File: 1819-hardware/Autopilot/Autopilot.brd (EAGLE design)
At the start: 44.4 x 54 mm, 36 parts, among them U1 PCA9615, U2 PCA9306, U3 74HC1G04, U4 MAX3485CSA, U5 V_REG_LD1117VXXLD1117-SMD

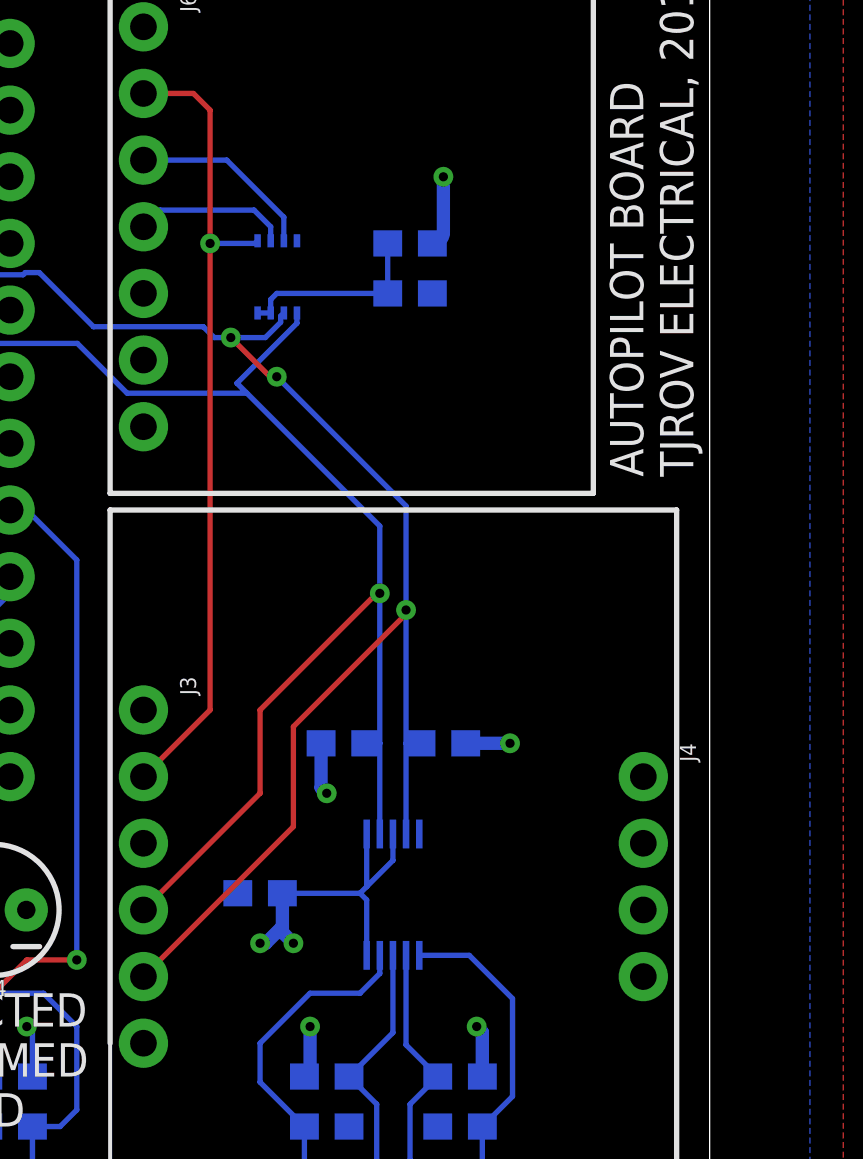
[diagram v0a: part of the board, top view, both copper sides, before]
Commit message: updated boards
700mil spacing on BNO055
changed PCA9306 package to MSOP8
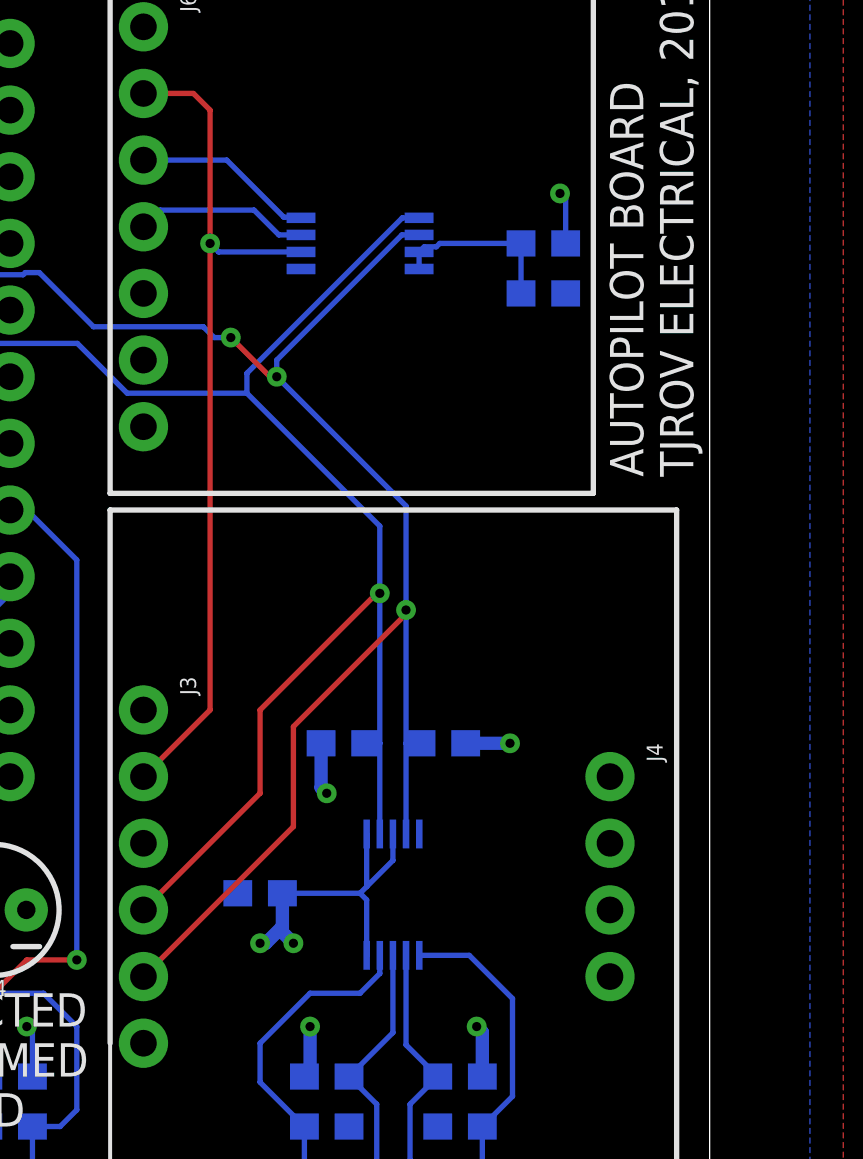
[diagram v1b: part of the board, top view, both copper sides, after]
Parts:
- U2: value PCA9306 -> (none); device SparkFun-IC-Comms:PSOP-8 -> SparkFun-IC-Comms:MSOP8
- moved C1 5.08 mm to (38.1, 39.4)
- moved R10 5.08 mm to (38.1, 41.3)
- moved U2 3.42 mm to (31.1, 41.3), turned to 90 degrees
- moved J4 1.27 mm to (40.6, 21.0)
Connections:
- net 3V3: now also U2.2; no longer U2.1
- net GND: now also U2.1; no longer U2.4
- net SCL3V3: now also U2.3; no longer U2.2
- net SDA3V3: now also U2.4; no longer U2.3
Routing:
- net SDA: track 52.2 -> 57.8 mm
- net SCL: track 55.4 -> 60.9 mm
- net 3V3: track 31.1 -> 32.9 mm
- net N$19: track 7.48 -> 6.57 mm
- net SCL3V3: track 5.91 -> 6.66 mm
- net VCC: track 35.5 -> 34.8 mm
